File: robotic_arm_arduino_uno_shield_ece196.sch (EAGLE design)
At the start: 37 parts, among them J1 (ID,OD)=(2.1,5.5)MM, J2 1x06-VERT-MALE, J3 1x06-VERT-MALE, J4 1x08-VERT-MALE, J5 1x08-VERT-MALE

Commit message: Updated ECE196 board.  Made a bit smaller
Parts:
- C0: device MrSwirlyEyes:CAP_POLARIZED_ALUM-ELECTROLYTIC_SMD_220UF-16V-20% -> PiB_capacitors:220UF-POLARIZED_SMD_16V-20%
- C1, C2: device MrSwirlyEyes:CAP_CERAMIC_SMD-805_0.22UF-50V-10% -> PiB_capacitors:0.22UF_SMD-805_50V-10%
- C3, C4: device MrSwirlyEyes:CAP_CERAMIC_SMD-805_0.1UF-50V-10% -> PiB_capacitors:0.1UF_SMD-805_50V-10%
- C5, C6: device MrSwirlyEyes:CAP_POLARIZED_ALUM-ELECTROLYTIC_SMD_100UF-16V-20% -> PiB_capacitors:100UF-POLARIZED_SMD_16V-20%
- D4, D5: device MrSwirlyEyes:DIODE_GEN-PURPSMD_GP_1A-50V-SOD123F -> PiB_discrete_semiconductors:DIODE_GENERAL-PURPOSE_SMD_GP_1A-50V
- J1: device MrSwirlyEyes:POWER_JACK-BARREL_ID2.1MM-OD5.5MM -> PiB_connectors:POWER_JACK-BARREL_ID2.1MM-OD5.5MM
- J2, J3: value 1x06-VERT-MALE -> 1x06-VERT-FEMALE; device connectors:1X06VERT-MALE -> PiB_connectors:1X06_VERT-FEMALE
- J4, J5: value 1x08-VERT-MALE -> 1x08-VERT-FEMALE; device connectors:1X08VERT-MALE -> PiB_connectors:1X08_VERT-FEMALE
- LIPO: value BATTERYPTH_HOLES -> 7.4V; device MrSwirlyEyes:BATTERYPTH_HOLES -> PiB_batteries:BATTERY_LIPO_BATTERY
- PLAY_LED: device MrSwirlyEyes:LED_SMD-805_DISCRETE_GREEN -> PiB_leds:LED_SMD-0805_DISCRETE_GREEN
- POT1, POT2, POT3, POT4: value 20KΩ -> 10KΩ; device MrSwirlyEyes:POTENTIOMETERNO-MARKINGS_VERT-FEMALE -> PiB_resistors:POTENTIOMETER_NO-MARKINGS_VERT-FEMALE
- PWR_LED: device MrSwirlyEyes:LED_SMD-805_DISCRETE_BLUE -> PiB_leds:LED_SMD-0805_DISCRETE_BLUE
- R0, R1, R2: device MrSwirlyEyes:RESISTORSMD-0805_1/8W_10K_5% -> PiB_resistors:10KΩ_SMD-0805_1/8W-5%
- R3: value 2KΩ -> 1KΩ; device MrSwirlyEyes:RESISTORSMD-0805_1/8W_2K_5% -> PiB_resistors:1KΩ_SMD-0805_1/8W-5%
- R4: device MrSwirlyEyes:RESISTORSMD-0805_1/8W_1K_5% -> PiB_resistors:1KΩ_SMD-0805_1/8W-5%
- REC_LED: device MrSwirlyEyes:LED_SMD-805_DISCRETE_RED -> PiB_leds:LED_SMD-0805_DISCRETE_RED
- S1: device MrSwirlyEyes:SWITCH_SPDT5A-28V_13L-7W -> PiB_switches:SWITCH_SPDT_VERT_PTH_5A-28V_13L-7W
- S2, S3: device MrSwirlyEyes:SWITCH_MOMENTARY_SPSTSPST-PTH-L12-W12-H7.2 -> PiB_switches:SWITCH_MOMENTARYSPST-PTH-L12-W12-H7.2
- SERVO1, SERVO2, SERVO3, SERVO4: device MrSwirlyEyes:SERVOMG90S_NO-MARKINGS -> PiB:SERVOMG90S
- SUPPLY14: device SparkFun-PowerSymbols:2PT_GND_TIE -> PiB_power_symbols:2PT_GND_TIE
- VREG1, VREG2: value 1.5A/5V -> LM340MP-5 1.5A/5V; device MrSwirlyEyes:VREG_LM340_LDO_1.5A-5V -> PiB_ic_power:VREG_LINEAR_FIXED_LM340MP-5_1.5A-5V
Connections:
- new net VCC: C0.A, C1.1, C2.1, D4.K, D5.K, PWR_LED.A, S1.1, VREG1.VI, VREG2.VI
- net +: now also S1.2; no longer S1.P
- net VIN: no longer C0.A, C1.1, C2.1, D4.K, D5.K, PWR_LED.A, S1.S1, VREG1.VI, VREG2.VI
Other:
- moved on the sheet: VREG1, VREG2

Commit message: Small corrections.
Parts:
- removed J2, J3: 1x06-VERT-FEMALE, PiB_connectors:1X06_VERT-FEMALE
- removed J4, J5: 1x08-VERT-FEMALE, PiB_connectors:1X08_VERT-FEMALE
- added ARDUINO1: Arduino UNO R3, PiB_boards:ARDUINO_UNO_R3_NO-HOLES_NO-AVR-ISP_NO-I2C_NO-NC_NO-IOREF
- J1: device PiB_connectors:POWER_JACK-BARREL_ID2.1MM-OD5.5MM -> PiB_connectors:POWER_JACK-BARREL_ID2.1MM-OD5.5MMPTH
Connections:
- removed net A4: J3.2
- removed net A5: J3.1
- removed net VCC: C0.A, C1.1, C2.1, D4.K, D5.K, PWR_LED.A, S1.1, VREG1.VI, VREG2.VI
- new net N$29: ARDUINO1.A0
- new net N$30: ARDUINO1.A1
- new net N$31: ARDUINO1.A2
- new net N$32: ARDUINO1.A3
- new net N$33: ARDUINO1.A4
- new net N$34: ARDUINO1.A5
- net 3.3V: now also ARDUINO1.3.3V; no longer J2.2
- net 5V: now also ARDUINO1.5V; no longer J2.3
- net A0: no longer J3.6
- net A1: no longer J3.5
- net A2: no longer J3.4
- net A3: no longer J3.3
- net AREF: now also ARDUINO1.AREF; no longer J5.8
- net D10: now also ARDUINO1.~D10; no longer J5.3
- net D11: now also ARDUINO1.~D11; no longer J5.4
- net D12: now also ARDUINO1.D12; no longer J5.5
- net D13: now also ARDUINO1.D13; no longer J5.6
- net D2: now also ARDUINO1.D2; no longer J4.3
- net D3: now also ARDUINO1.~D3; no longer J4.4
- net D4: now also ARDUINO1.D4; no longer J4.5
- net D5: now also ARDUINO1.~D5; no longer J4.6
- net D6: now also ARDUINO1.~D6; no longer J4.7
- net D7: now also ARDUINO1.D7; no longer J4.8
- net D8: now also ARDUINO1.D8; no longer J5.1
- net D9: now also ARDUINO1.~D9; no longer J5.2
- net GND: now also ARDUINO1.GND@0, ARDUINO1.GND@1, ARDUINO1.GND@2; no longer J2.4, J2.5, J5.7
- net RESET: now also ARDUINO1.!RESET!@1; no longer J2.1
- net RX: now also ARDUINO1.RX->D0; no longer J4.1
- net TX: now also ARDUINO1.TX->D1; no longer J4.2
- net VIN: now also ARDUINO1.VIN, C0.A, C1.1, C2.1, D4.K, D5.K, PWR_LED.A, S1.1, VREG1.VI, VREG2.VI; no longer J2.6

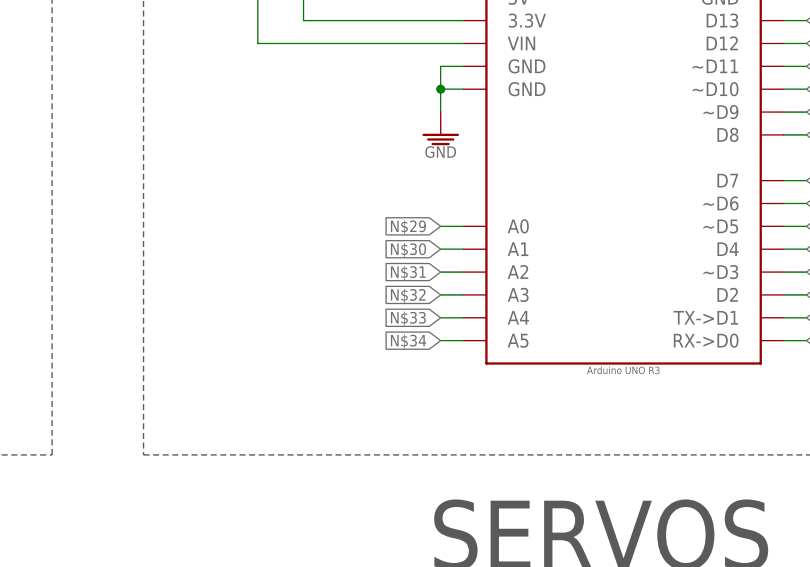
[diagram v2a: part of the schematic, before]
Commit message: Rev 4: Fixed error not connecting analog pins.  Ready for fab.
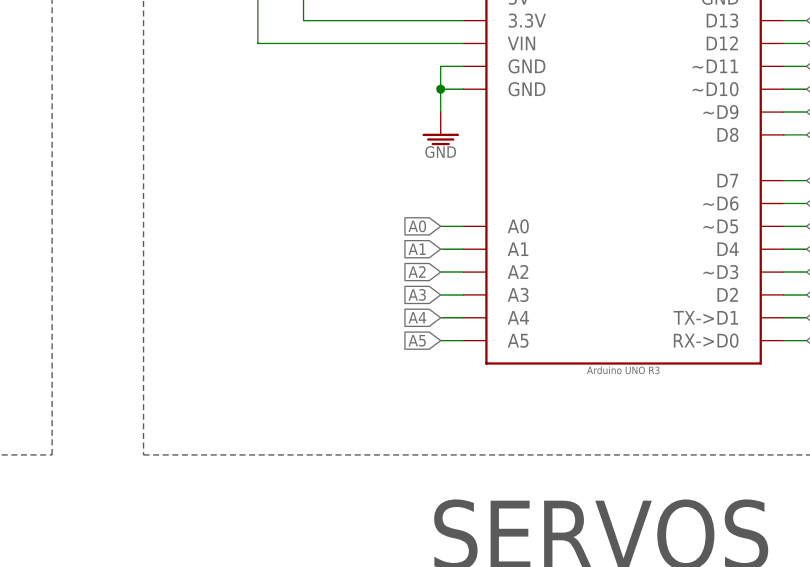
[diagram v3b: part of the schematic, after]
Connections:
- net N$33 renamed A4
- net N$34 renamed A5
- removed net N$29: ARDUINO1.A0
- removed net N$30: ARDUINO1.A1
- removed net N$31: ARDUINO1.A2
- removed net N$32: ARDUINO1.A3
- net A0: now also ARDUINO1.A0
- net A1: now also ARDUINO1.A1
- net A2: now also ARDUINO1.A2
- net A3: now also ARDUINO1.A3
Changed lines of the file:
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@@
 <pinref part="POT1" gate="G$1" pin="S"/>
+</segment>
+<segment>
+<wire x1="213.36" y1="73.66" x2="215.9" y2="73.66" width="0.1524" layer="91"/>
+<label x="213.36" y="73.66" size="1.27" layer="95" font="vector" ratio="10" rot="R180" xref="yes"/>
+<pinref part="ARDUINO1" gate="G$1" pin="A0"/>
 </segment>
 </net>
@@
 <pinref part="POT2" gate="G$1" pin="S"/>
 </segment>
+<segment>
+<wire x1="213.36" y1="71.12" x2="215.9" y2="71.12" width="0.1524" layer="91"/>
+<label x="213.36" y="71.12" size="1.27" layer="95" font="vector" ratio="10" rot="R180" xref="yes"/>
+<pinref part="ARDUINO1" gate="G$1" pin="A1"/>
+</segment>
 </net>
 <net name="A2" class="0">
@@
 <pinref part="POT3" gate="G$1" pin="S"/>
 </segment>
+<segment>
+<wire x1="213.36" y1="68.58" x2="215.9" y2="68.58" width="0.1524" layer="91"/>
+<label x="213.36" y="68.58" size="1.27" layer="95" font="vector" ratio="10" rot="R180" xref="yes"/>
+<pinref part="ARDUINO1" gate="G$1" pin="A2"/>
+</segment>
 </net>
 <net name="A3" class="0">
@@
 <pinref part="POT4" gate="G$1" pin="S"/>
 <wire x1="271.78" y1="-30.48" x2="274.32" y2="-30.48" width="0.1524" layer="91"/>
+</segment>
+<segment>
+<wire x1="213.36" y1="66.04" x2="215.9" y2="66.04" width="0.1524" layer="91"/>
+<label x="213.36" y="66.04" size="1.27" layer="95" font="vector" ratio="10" rot="R180" xref="yes"/>
+<pinref part="ARDUINO1" gate="G$1" pin="A3"/>
 </segment>
 </net>
@@
 </segment>
 </net>
-<net name="N$29" class="0">
-<segment>
-<wire x1="213.36" y1="73.66" x2="215.9" y2="73.66" width="0.1524" layer="91"/>
-<label x="213.36" y="73.66" size="1.27" layer="95" font="vector" ratio="10" rot="R180" xref="yes"/>
-<pinref part="ARDUINO1" gate="G$1" pin="A0"/>
-</segment>
-</net>
-<net name="N$30" class="0">
-<segment>
-<wire x1="213.36" y1="71.12" x2="215.9" y2="71.12" width="0.1524" layer="91"/>
-<label x="213.36" y="71.12" size="1.27" layer="95" font="vector" ratio="10" rot="R180" xref="yes"/>
-<pinref part="ARDUINO1" gate="G$1" pin="A1"/>
-</segment>
-</net>
-<net name="N$31" class="0">
-<segment>
-<wire x1="213.36" y1="68.58" x2="215.9" y2="68.58" width="0.1524" layer="91"/>
-<label x="213.36" y="68.58" size="1.27" layer="95" font="vector" ratio="10" rot="R180" xref="yes"/>
-<pinref part="ARDUINO1" gate="G$1" pin="A2"/>
-</segment>
-</net>
-<net name="N$32" class="0">
-<segment>
-<wire x1="213.36" y1="66.04" x2="215.9" y2="66.04" width="0.1524" layer="91"/>
-<label x="213.36" y="66.04" size="1.27" layer="95" font="vector" ratio="10" rot="R180" xref="yes"/>
-<pinref part="ARDUINO1" gate="G$1" pin="A3"/>
-</segment>
-</net>
-<net name="N$33" class="0">
+<net name="A4" class="0">
 <segment>
 <wire x1="213.36" y1="63.5" x2="215.9" y2="63.5" width="0.1524" layer="91"/>
@@
 </segment>
 </net>
-<net name="N$34" class="0">
+<net name="A5" class="0">
 <segment>
 <wire x1="213.36" y1="60.96" x2="215.9" y2="60.96" width="0.1524" layer="91"/>
